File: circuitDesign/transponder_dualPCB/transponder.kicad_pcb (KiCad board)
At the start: 2 copper layers, 46.7 x 22.9 mm, 26 parts, among them IC1 ATTINY85-P, IC2 ATTINY85-P, J1 Conn_01x02, J2 Conn_01x03, P1 CONN_2, P2 CONN_2, U1 L78L05_SOT89, U2 L78L05_SOT89, X1 CRYSTAL, X2 CRYSTAL

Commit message: PCB print version
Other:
- board text added: "github.com/condac/openAST"
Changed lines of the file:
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@@
     (area 94.945999 100.279999 141.782001 123.240001)
     (thickness 1.6)
-    (drawings 17)
+    (drawings 19)
     (tracks 239)
     (zones 0)
@@
     )
   )
+  (gr_text github.com/condac/openAST (at 107.696 111.252 90) (layer B.SilkS)
+    (effects (font (size 0.75 0.75) (thickness 0.1875)) (justify mirror))
+  )
+  (gr_text github.com/condac/openAST (at 130.175 114.935) (layer B.SilkS)
+    (effects (font (size 0.75 0.75) (thickness 0.1875)) (justify mirror))
+  )
   (gr_line (start 117.856 104.902) (end 118.872 104.902) (angle 90) (layer Edge.Cuts) (width 0.1))

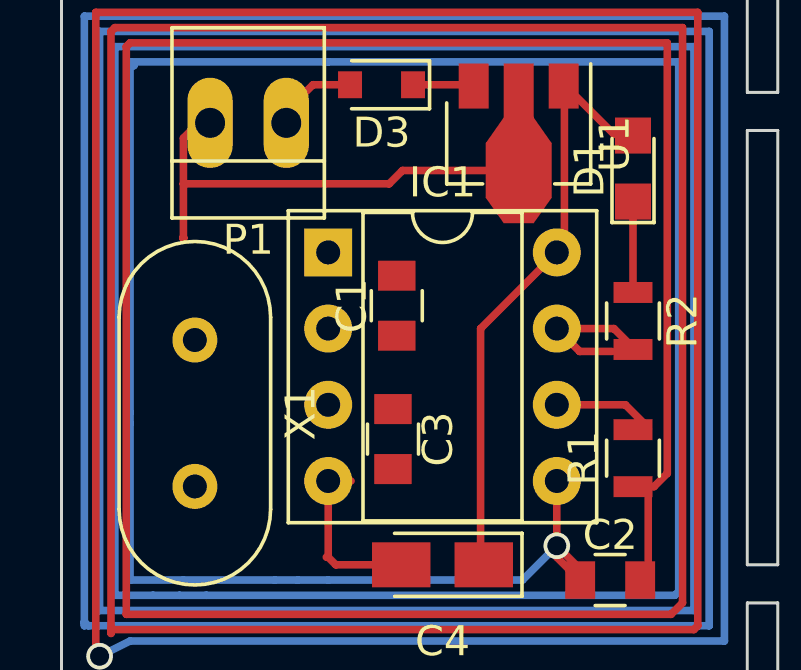
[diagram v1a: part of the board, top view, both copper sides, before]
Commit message: PCB print version
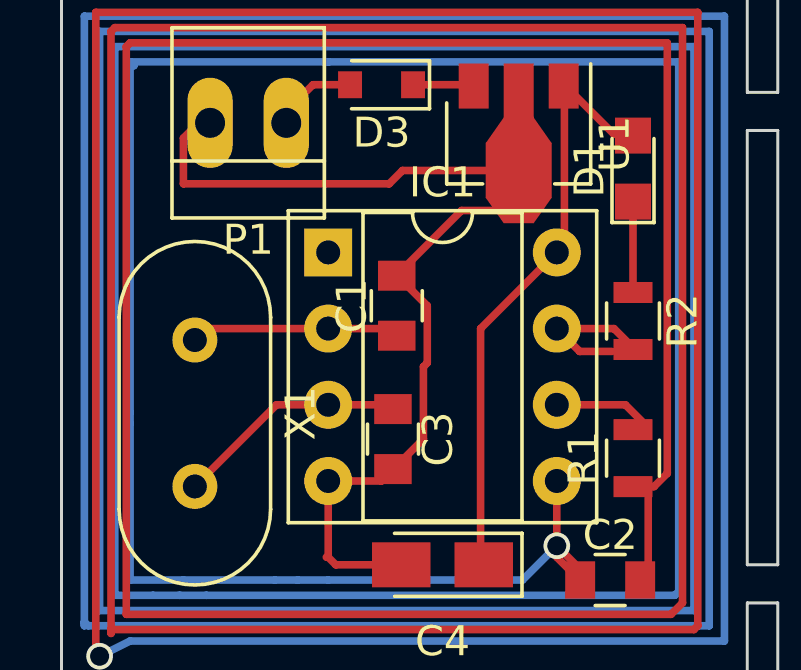
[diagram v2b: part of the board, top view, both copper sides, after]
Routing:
- net GND: track 52.3 -> 64.9 mm
- net Net-(C3-Pad1): track 0.00 -> 7.85 mm
- net Net-(C1-Pad1): track 0.00 -> 7.55 mm
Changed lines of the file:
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@@
   (general
     (links 52)
-    (no_connects 12)
+    (no_connects 5)
     (area 94.945999 100.279999 141.782001 123.240001)
     (thickness 1.6)
     (drawings 19)
-    (tracks 239)
+    (tracks 258)
     (zones 0)
     (modules 26)
@@
     (visible_elements FFFFFF9F)
     (pcbplotparams
-      (layerselection 0x00030_80000001)
+      (layerselection 0x010f0_80000001)
       (usegerberextensions true)
       (excludeedgelayer true)
@@
       (outputformat 1)
       (mirror false)
-      (drillshape 1)
+      (drillshape 0)
       (scaleselection 1)
-      (outputdirectory ""))
+      (outputdirectory plots/))
   )
   (net 0 "")
@@
   (segment (start 103.886 108.966) (end 104.394 108.458) (width 0.254) (layer F.Cu) (net 0) (status 80000))
   (segment (start 103.886 108.966) (end 104.394 108.458) (width 0.254) (layer F.Cu) (net 0) (status 80000))
+  (segment (start 106.045 116.189) (end 106.045 116.205) (width 0.254) (layer F.Cu) (net 1) (status 80000))
+  (segment (start 106.045 116.205) (end 105.664 116.586) (width 0.254) (layer F.Cu) (net 1) (status 80000))
+  (segment (start 105.664 116.586) (end 103.886 116.586) (width 0.254) (layer F.Cu) (net 1) (status 80000))
+  (segment (start 110.236 107.569) (end 108.331 107.569) (width 0.254) (layer F.Cu) (net 1) (status 80000))
+  (segment (start 108.331 107.569) (end 106.172 109.728) (width 0.254) (layer F.Cu) (net 1) (status 80000))
+  (segment (start 106.172 109.728) (end 106.172 109.744) (width 0.254) (layer F.Cu) (net 1) (status 80000))
+  (segment (start 106.172 109.744) (end 106.172 109.728) (width 0.254) (layer F.Cu) (net 1) (status 80000))
+  (segment (start 106.172 109.728) (end 107.188 110.744) (width 0.254) (layer F.Cu) (net 1) (status 80000))
+  (segment (start 107.188 110.744) (end 107.188 112.649) (width 0.254) (layer F.Cu) (net 1) (status 80000))
+  (segment (start 107.188 112.649) (end 107.061 112.776) (width 0.254) (layer F.Cu) (net 1) (status 80000))
+  (segment (start 107.061 112.776) (end 107.061 115.189) (width 0.254) (layer F.Cu) (net 1) (status 80000))
+  (segment (start 107.061 115.189) (end 106.045 116.205) (width 0.254) (layer F.Cu) (net 1) (status 80000))
+  (segment (start 106.045 116.205) (end 106.045 116.189) (width 0.254) (layer F.Cu) (net 1) (status 80000))
   (segment (start 103.87 119.126) (end 103.886 119.126) (width 0.254) (layer F.Cu) (net 1) (status 80000))
   (segment (start 103.886 119.126) (end 104.14 119.38) (width 0.254) (layer F.Cu) (net 1) (status 80000))
@@
   (segment (start 103.886 116.586) (end 104.648 116.586) (width 0.254) (layer F.Cu) (net 1))
   (segment (start 105.918 106.68) (end 99.06 106.68) (width 0.254) (layer F.Cu) (net 1))
-  (segment (start 99.06 108.474) (end 99.06 108.458) (width 0.254) (layer F.Cu) (net 1) (status 80000))
   (segment (start 99.822 104.394) (end 99.06 105.156) (width 0.254) (layer F.Cu) (net 1) (status 80000))
   (segment (start 99.06 105.156) (end 99.06 106.68) (width 0.254) (layer F.Cu) (net 1) (status 80000))
-  (segment (start 99.06 106.68) (end 99.06 108.474) (width 0.254) (layer F.Cu) (net 1) (status 80000))
   (segment (start 110.236 104.8258) (end 110.236 104.902) (width 0.254) (layer F.Cu) (net 1) (status 80000))
   (segment (start 110.236 104.8258) (end 110.236 106.2355) (width 0.254) (layer F.Cu) (net 1) (status 80000))
   (segment (start 110.236 104.8258) (end 110.236 103.5685) (width 0.254) (layer F.Cu) (net 1) (status 80000))
-  (segment (start 99.06 108.5215) (end 99.06 108.458) (width 0.254) (layer F.Cu) (net 1) (status 80000))
-  (segment (start 99.06 108.5215) (end 99.06 108.458) (width 0.254) (layer F.Cu) (net 1) (status 80000))
-  (segment (start 99.06 108.5215) (end 99.06 108.458) (width 0.254) (layer F.Cu) (net 1) (status 80000))
-  (segment (start 99.06 108.458) (end 99.06 108.5215) (width 0.254) (layer F.Cu) (net 1) (status 80000))
   (segment (start 103.886 116.586) (end 103.886 119.126) (width 0.254) (layer F.Cu) (net 1) (status 80000))
   (segment (start 103.886 119.126) (end 103.8225 119.126) (width 0.254) (layer F.Cu) (net 1) (status 80000))
@@
   (segment (start 131.445 114.046) (end 130.937 114.554) (width 0.254) (layer F.Cu) (net 1) (status 80000))
   (segment (start 130.937 114.554) (end 130.269 114.554) (width 0.254) (layer F.Cu) (net 1) (status 80000))
+  (segment (start 103.886 111.506) (end 99.822 111.506) (width 0.254) (layer F.Cu) (net 2) (status C00000))
+  (segment (start 99.822 111.506) (end 99.441 111.887) (width 0.254) (layer F.Cu) (net 2) (status C00000))
+  (segment (start 99.441 111.887) (end 99.822 111.506) (width 0.254) (layer B.Cu) (net 2) (status 80000))
+  (segment (start 103.886 111.506) (end 105.918 111.506) (width 0.254) (layer F.Cu) (net 2) (status 80000))
+  (segment (start 105.918 111.506) (end 106.172 111.76) (width 0.254) (layer F.Cu) (net 2) (status 80000))
+  (segment (start 106.172 111.76) (end 106.172 111.744) (width 0.254) (layer F.Cu) (net 2) (status 80000))
   (segment (start 103.886 102.616) (end 97.282 102.616) (width 0.254) (layer B.Cu) (net 3))
   (segment (start 114.747 116.774) (end 115.189 116.332) (width 0.254) (layer F.Cu) (net 3))
@@
   (segment (start 114.3 119.888) (end 114.554 119.634) (width 0.254) (layer F.Cu) (net 3) (status 80000))
   (segment (start 114.554 119.634) (end 114.554 116.7765) (width 0.254) (layer F.Cu) (net 3) (status 80000))
+  (segment (start 103.886 114.046) (end 102.162 114.046) (width 0.254) (layer F.Cu) (net 4) (status 400000))
+  (segment (start 102.162 114.046) (end 99.441 116.767) (width 0.254) (layer F.Cu) (net 4) (status 800000))
+  (segment (start 99.441 116.767) (end 99.441 116.713) (width 0.254) (layer B.Cu) (net 4) (status 80000))
+  (segment (start 103.886 114.046) (end 105.918 114.046) (width 0.254) (layer F.Cu) (net 4) (status 80000))
+  (segment (start 105.918 114.046) (end 106.045 114.173) (width 0.254) (layer F.Cu) (net 4) (status 80000))
+  (segment (start 106.045 114.173) (end 106.045 114.189) (width 0.254) (layer F.Cu) (net 4) (status 80000))
   (segment (start 111.736 103.422) (end 111.76 103.378) (width 0.254) (layer F.Cu) (net 5) (status 80000))
   (segment (start 111.76 103.378) (end 113.411 105.029) (width 0.254) (layer F.Cu) (net 5) (status 80000))
